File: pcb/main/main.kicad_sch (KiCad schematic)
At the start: 2 parts, among them J1 XT60PW-M

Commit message: feat: finish main board v2
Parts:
- J1: footprint Connector_AMASS:AMASS_XT60-F_1x02_P7.20mm_Vertical -> Connector_AMASS:AMASS_XT60PW-F_1x02_P7.20mm_Horizontal
- renumbered C17 to C1
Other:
- sheet power ports: added ADC_BATTERY; removed none
- sheet stm32f405rg ports: added ADC_BATTERY, SPI2_CLK, SPI2_MISO, SPI2_MOSI; removed SPI3_CLK, SPI3_MISO, SPI3_MOSI

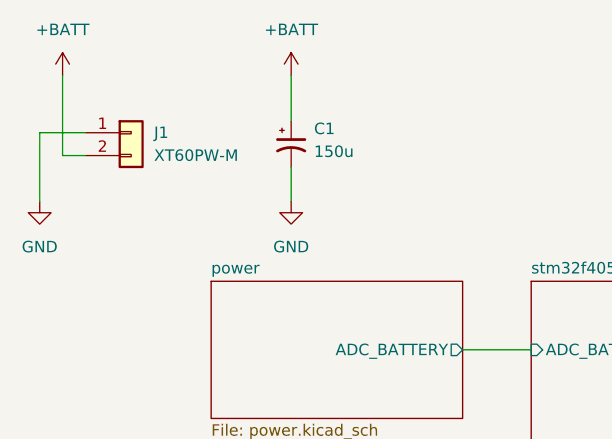
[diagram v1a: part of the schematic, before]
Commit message: feat: delete two CAN connectors & add microSD input pin
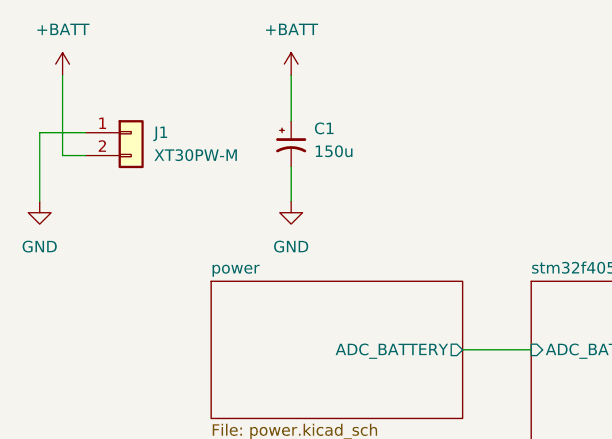
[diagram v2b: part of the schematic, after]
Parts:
- J1: value XT60PW-M -> XT30PW-M; footprint Connector_AMASS:AMASS_XT60PW-F_1x02_P7.20mm_Horizontal -> Connector_AMASS:AMASS_XT30PW-M_1x02_P2.50mm_Horizontal
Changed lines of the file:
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@@
 			)
 		)
-		(property "Value" "XT60PW-M"
+		(property "Value" "XT30PW-M"
 			(at 67.31 48.2599 0)
 			(effects
@@
 			)
 		)
-		(property "Footprint" "Connector_AMASS:AMASS_XT60PW-F_1x02_P7.20mm_Horizontal"
+		(property "Footprint" "Connector_AMASS:AMASS_XT30PW-M_1x02_P2.50mm_Horizontal"
 			(at 64.77 45.72 0)
 			(effects
